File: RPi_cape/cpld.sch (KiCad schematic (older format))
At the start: 59 parts, among them J15 Conn_02x05_Odd_Even, Q10 MMBT3904, Q9 MMBT3904, U29 LP5907MFX-3.3, U30 LP5907MFX-1.8, U31 5M40ZE64, U32 MIC1557, U33 5M80ZT100 / 5M240ZT100

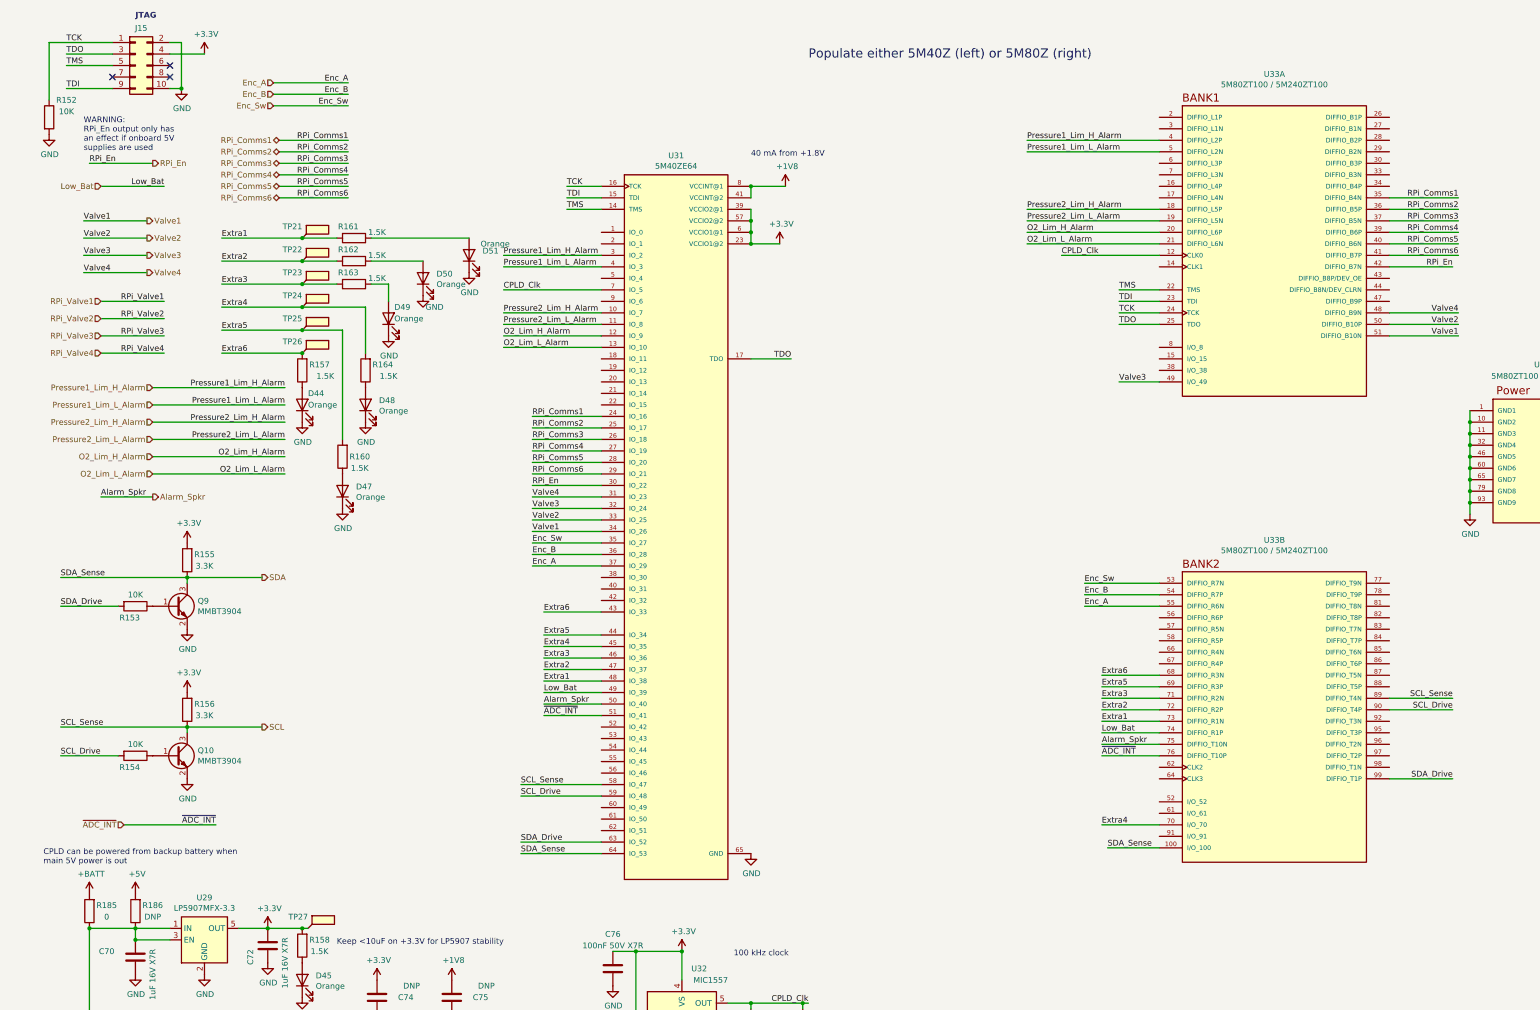
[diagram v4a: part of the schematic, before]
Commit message: Better valve monitoring, finalized layout and manufacturing files
Created assembly and fabrication drawings, assigned all BOM parts, generally made design ready for ordering
Added strain-relief slots and barb mounting dimensions for digital pressure sensors
Changed valve drivers from discrete power MOSFETs to "smart" industrial/automotive driver ICs for the current monitoring, including valve-movement monitor for #4
Connected RPi_Valve* signals to larger CPLD footprint, changed Raspberry Pi pin assignment as a result to ease PCB routing
Updated footprints, page layout to create readable assembly drawing
Added current-measurement testpoints for CPLD power from BATT+
Changed power diodes in power-down-alarm circuit to small-signal parts for more compact layout
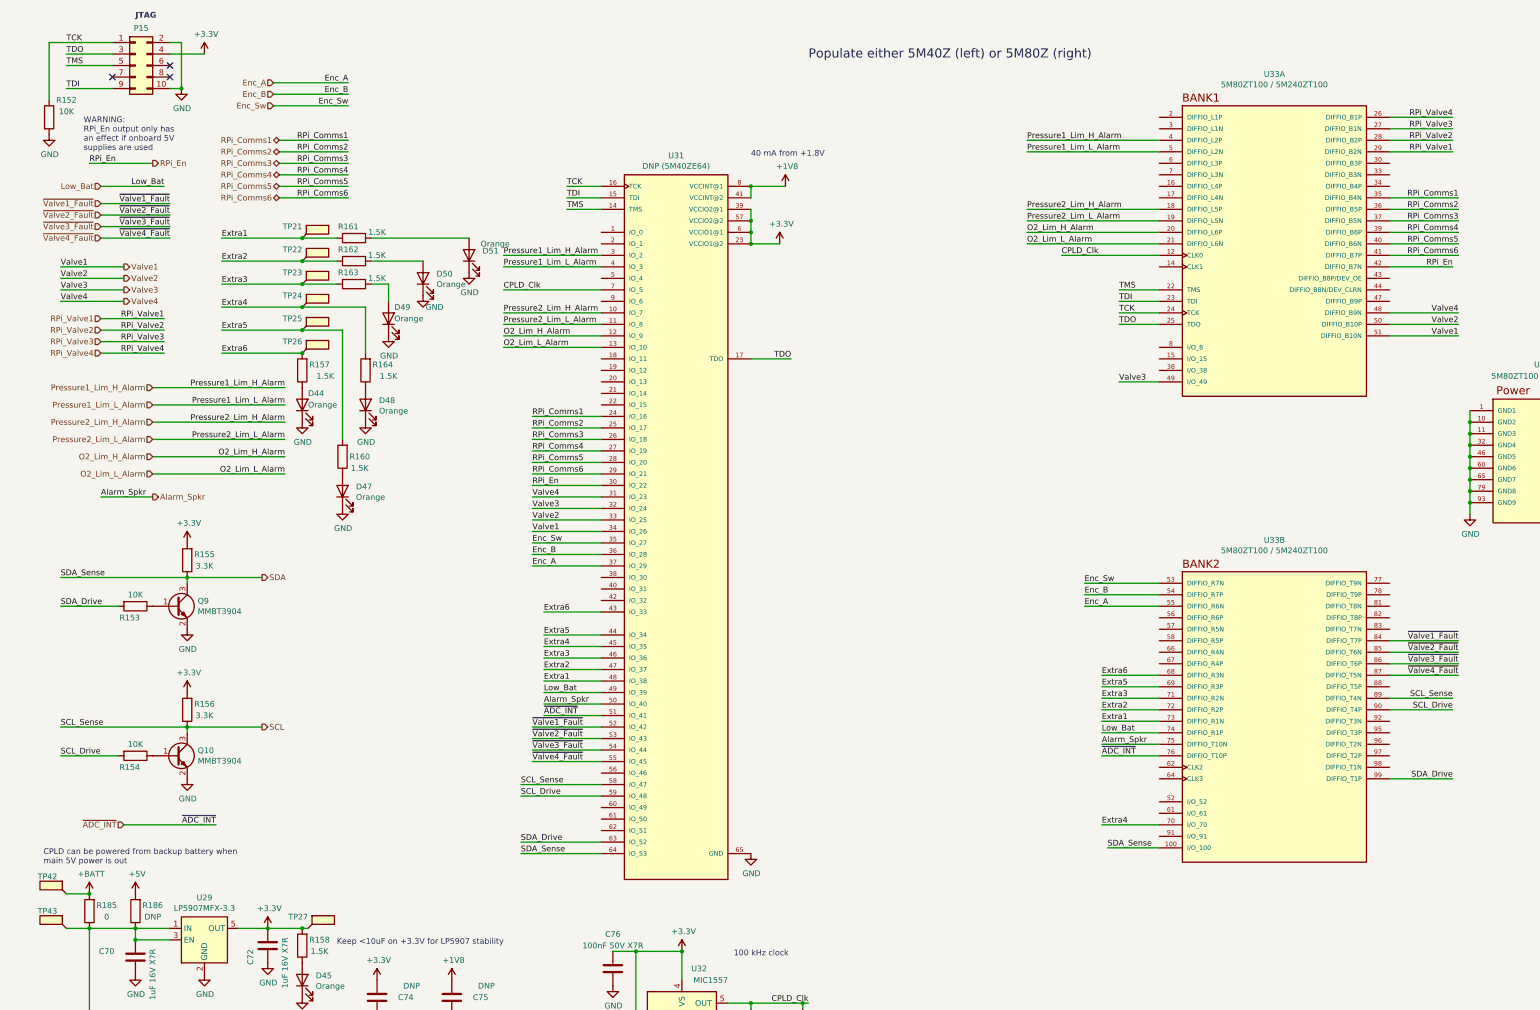
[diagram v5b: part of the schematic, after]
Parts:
- added TP42, TP43: TestPoint_Flag, TestPoint:TestPoint_Keystone_5019_Minature, symbol Connector:TestPoint_Flag
- C79: Manufacturer AVX -> Murata; Part Number 06035A102JAT2A -> GRM1885C1H103JA01D
- D44, D45, D46, D47, D48, D49, D50, D51: footprint LED_SMD:LED_0805_2012Metric -> Ventilator:LED_0805_2012Metric
- Q10, Q9: footprint Package_TO_SOT_SMD:SOT-23 -> Ventilator:SOT-23; Manufacturer (none) -> Diodes Inc.; Part Number (none) -> MMBT3904-7-F
- R152, R153, R154, R165: Manufacturer (none) -> KOA Speer; Part Number (none) -> RK73H2BTTD1002F
- R155, R156: Manufacturer (none) -> KOA Speer; Part Number (none) -> RK73H2BTTD3301F
- R157, R158, R160, R161, R162, R163, R164: Manufacturer (none) -> KOA Speer; Part Number (none) -> RK73H2BTTD1501F
- R159: Manufacturer (none) -> KOA Speer; Part Number (none) -> RK73H2BTTD1000F
- R166: Manufacturer (none) -> KOA Speer; Part Number (none) -> RK73H2BTTD2492F
- R185: Manufacturer (none) -> Panasonic; Part Number (none) -> ERJ-8GEY0R00V
- U29, U30, U32: footprint Package_TO_SOT_SMD:SOT-23-5 -> Ventilator:SOT-23-5
- U31: value 5M40ZE64 -> DNP (5M40ZE64)
- U33: Manufacturer (none) -> Intel; Part Number (none) -> 5M240ZT100I5N
- renumbered J15 to P15
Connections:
- net +BATT: now also TP42.1
- net RPi_Valve1: now also U33.29 (DIFFIO_B2N)
- net RPi_Valve2: now also U33.28 (DIFFIO_B2P)
- net RPi_Valve3: now also U33.27 (DIFFIO_B1N)
- net RPi_Valve4: now also U33.26 (DIFFIO_B1P)
- net ~Valve1_Fault: now reaches U31.52 (IO_42)
- net ~Valve1_Fault: now also U33.84 (DIFFIO_T7P)
- net ~Valve2_Fault: now reaches U31.53 (IO_43)
- net ~Valve2_Fault: now also U33.85 (DIFFIO_T6N)
- net ~Valve3_Fault: now reaches U31.54 (IO_44)
- net ~Valve3_Fault: now also U33.86 (DIFFIO_T6P)
- net ~Valve4_Fault: now reaches U31.55 (IO_45)
- net ~Valve4_Fault: now also U33.87 (DIFFIO_T5N)
- net at C70.2, C71.2, R185.1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: now also TP43.1

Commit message: Manufacturing clean-up
Corrections and additions to BOM etc. for manufacturing
Added power draw tracking spreadsheet
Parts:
- C79: Manufacturer Murata -> AVX; Part Number GRM1885C1H103JA01D -> 06035A102JAT2A
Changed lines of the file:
@@
 F 2 "Capacitor_SMD:C_0603_1608Metric" H 6788 9700 50  0001 C CNN
 F 3 "~" H 6750 9850 50  0001 C CNN
-F 4 "Murata" H 6750 9850 50  0001 C CNN "Manufacturer"
-F 5 "GRM1885C1H103JA01D" H 6750 9850 50  0001 C CNN "Part Number"
+F 4 "AVX" H 6750 9850 50  0001 C CNN "Manufacturer"
+F 5 "06035A102JAT2A" H 6750 9850 50  0001 C CNN "Part Number"
 	1    6750 9850
 	-1   0    0    1

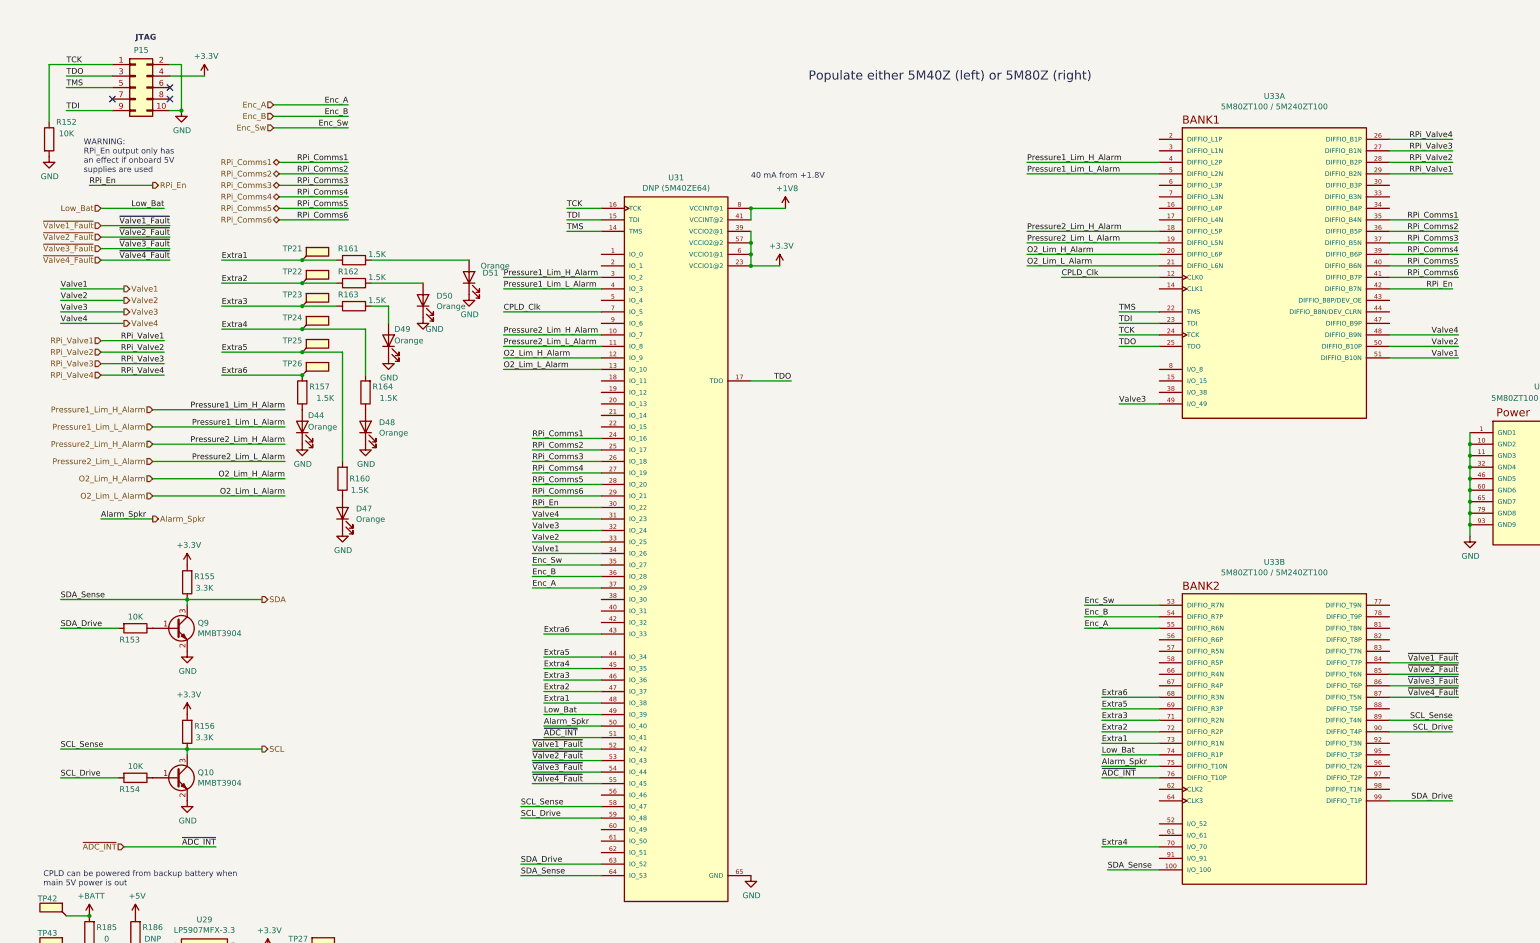
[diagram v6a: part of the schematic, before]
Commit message: Safety additions
Switched CPLD_ADC7 to +24V monitoring (from +5V monitoring), and added CPLD ~Bat_On digital input(s) to know when it's running from backup battery, to cover low-input-voltage edge cases
Added series 1K resistors (R226-231) on CPLD<->RPi Comms1-6 lines, to protect CPLD in case of overvoltage from RPi failure
Added optional input TVS D23 to handle sustained over-voltage or large surges
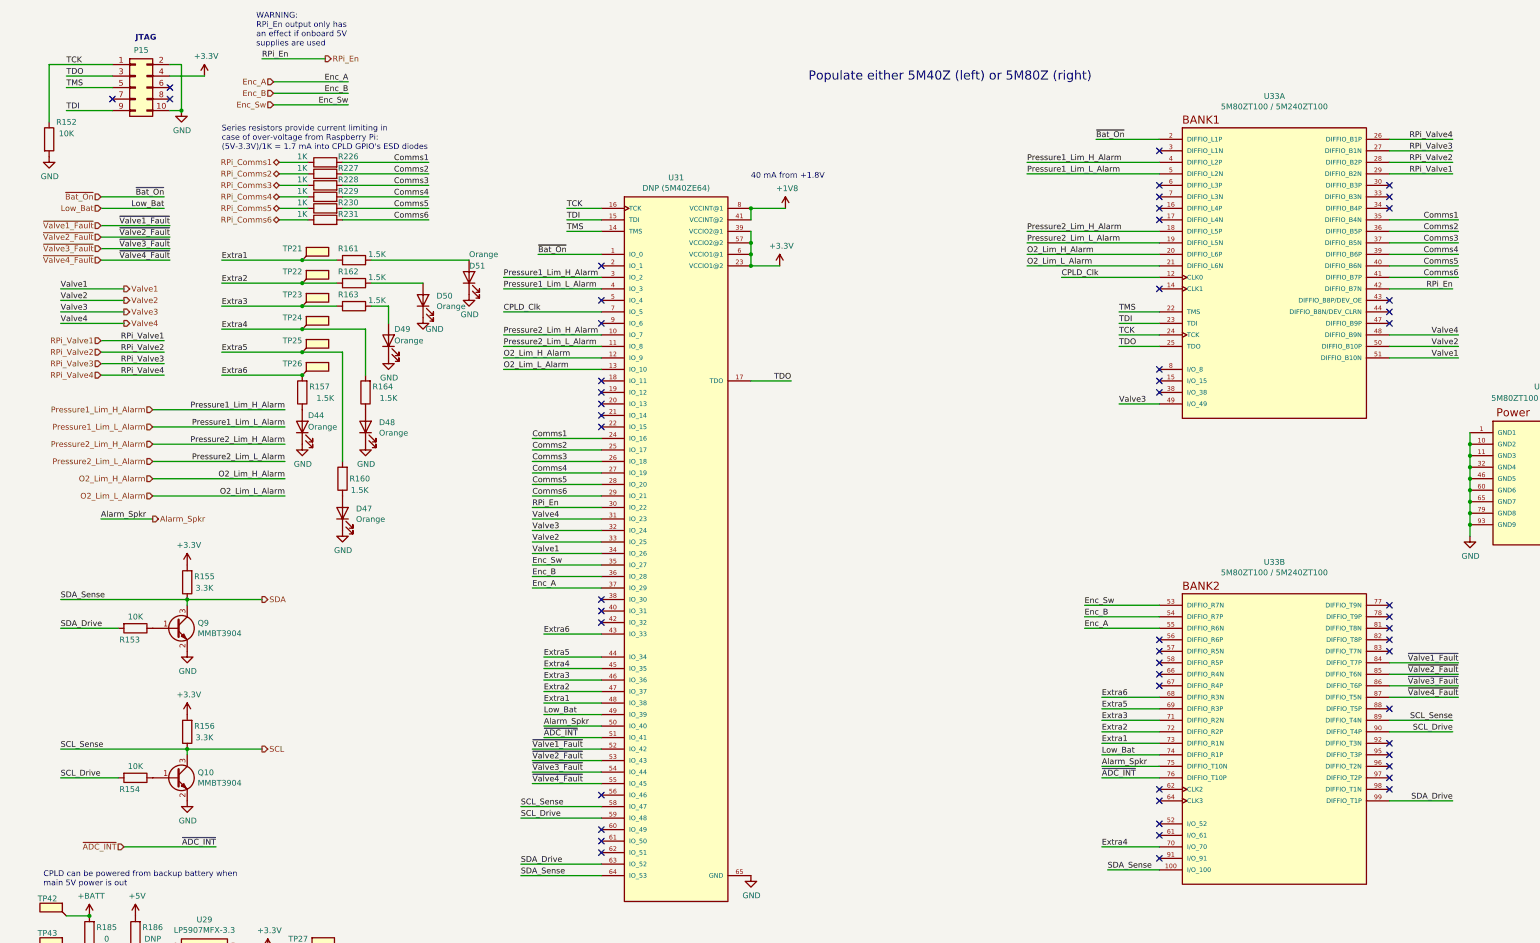
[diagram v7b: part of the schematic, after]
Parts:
- added R226, R227, R228, R229, R230, R231: 1K, Resistor_SMD:R_1206_3216Metric, symbol Device:R
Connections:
- net RPi_Comms1: now also R226.1; no longer U31.24 (IO_16), U33.35 (DIFFIO_B4N)
- net RPi_Comms2: now also R227.1; no longer U31.25 (IO_17), U33.36 (DIFFIO_B5P)
- net RPi_Comms3: now also R228.1; no longer U31.26 (IO_18), U33.37 (DIFFIO_B5N)
- net RPi_Comms4: now also R229.1; no longer U31.27 (IO_19), U33.39 (DIFFIO_B6P)
- net RPi_Comms5: now also R230.1; no longer U31.28 (IO_20), U33.40 (DIFFIO_B6N)
- net RPi_Comms6: now also R231.1; no longer U31.29 (IO_21), U33.41 (DIFFIO_B7P)
- net ~Bat_On: now reaches U31.1 (IO_0)
- net ~Bat_On: now also U33.2 (DIFFIO_L1P)
- new net Comms1: R226.2, U31.24 (IO_16), U33.35 (DIFFIO_B4N)
- new net Comms2: R227.2, U31.25 (IO_17), U33.36 (DIFFIO_B5P)
- new net Comms3: R228.2, U31.26 (IO_18), U33.37 (DIFFIO_B5N)
- new net Comms4: R229.2, U31.27 (IO_19), U33.39 (DIFFIO_B6P)
- new net Comms5: R230.2, U31.28 (IO_20), U33.40 (DIFFIO_B6N)
- new net Comms6: R231.2, U31.29 (IO_21), U33.41 (DIFFIO_B7P)
- no-connect marks 3 -> 54
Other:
- note added: "Series resistors provide current limiting in\ncase of over-voltage from Raspberry Pi:\n(5V-3.3V)/1K = 1.7 mA into CPLD GPIO's ESD diodes"

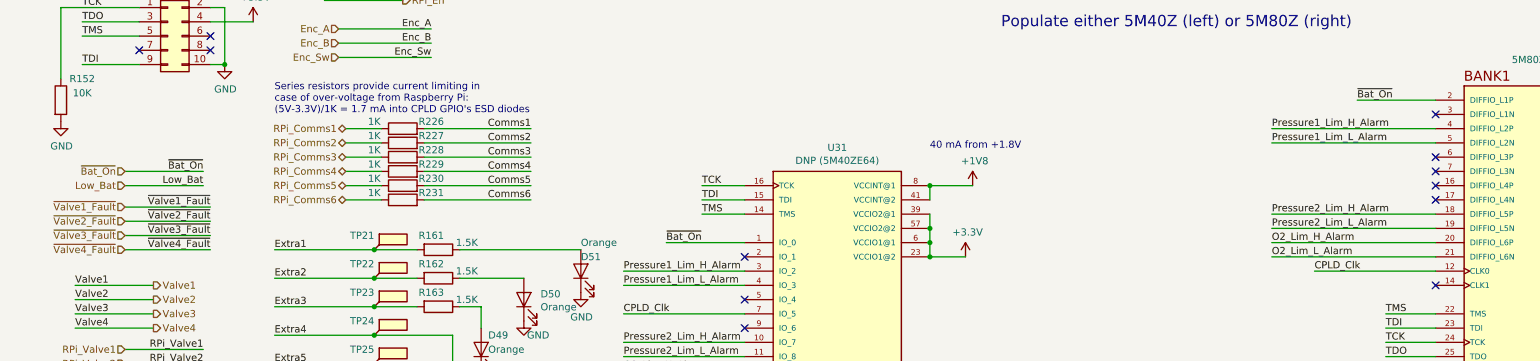
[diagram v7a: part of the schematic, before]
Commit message: +5VA outage detection
Separated +1.8V and +5VA monitoring and added +3.3V output for +5VA on ~5VA_On signal to CPLD, to cover an extra failure mode
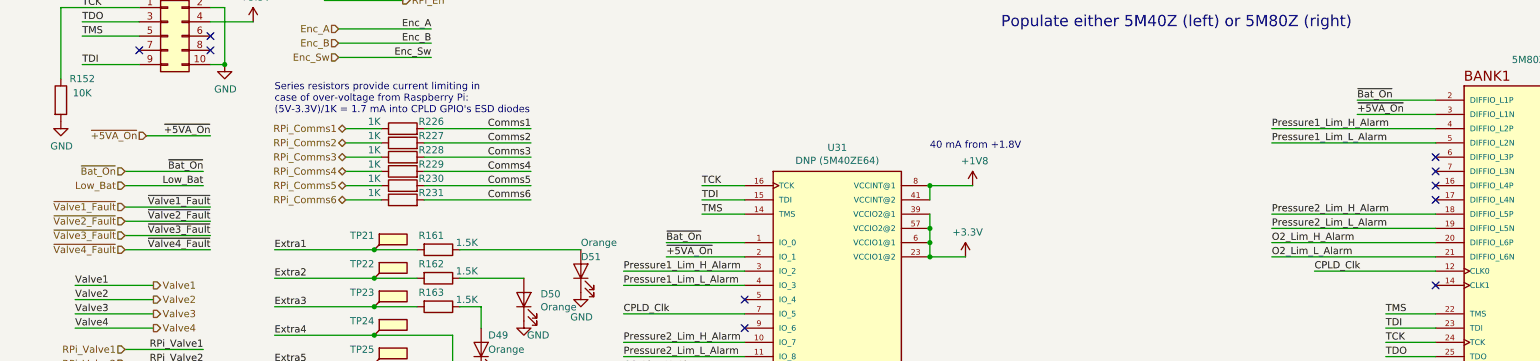
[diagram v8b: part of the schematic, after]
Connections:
- net ~+5VA_On: now reaches U31.2 (IO_1)
- net ~+5VA_On: now also U33.3 (DIFFIO_L1N)
- no-connect marks 54 -> 52
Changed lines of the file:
@@
 Title "CPLD"
 Date ""
-Rev "1.6"
+Rev "1.7"
 Comp "Partners COVID Innovation Group"
 Comment1 "Don Straney"
@@
 Text Label 9750 1600 0    50   ~ 0
 ~Bat_On
-NoConn ~ 5450 2700
 NoConn ~ 5450 3000
 NoConn ~ 5450 3200
@@
 NoConn ~ 10300 6050
 NoConn ~ 10300 5950
-NoConn ~ 10300 1700
 NoConn ~ 10300 2000
 NoConn ~ 10300 2100
@@
 Text Notes 2150 1700 0    50   ~ 0
 Series resistors provide current limiting in\ncase of over-voltage from Raspberry Pi:\n(5V-3.3V)/1K = 1.7 mA into CPLD GPIO's ESD diodes
+Text HLabel 1250 1850 0    50   Input ~ 0
+~+5VA_On
+Wire Wire Line
+	1250 1850 1700 1850
+Text Label 1700 1850 2    50   ~ 0
+~+5VA_On
+Text Label 4900 2700 0    50   ~ 0
+~+5VA_On
+Wire Wire Line
+	4900 2700 5450 2700
+Text Label 9750 1700 0    50   ~ 0
+~+5VA_On
+Wire Wire Line
+	9750 1700 10300 1700
 $EndSCHEMATC
